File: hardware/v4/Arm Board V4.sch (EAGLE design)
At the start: 43 parts, among them U1 SN74LS241DW, U2 XBEE-1B3, U3 LSM9DS0

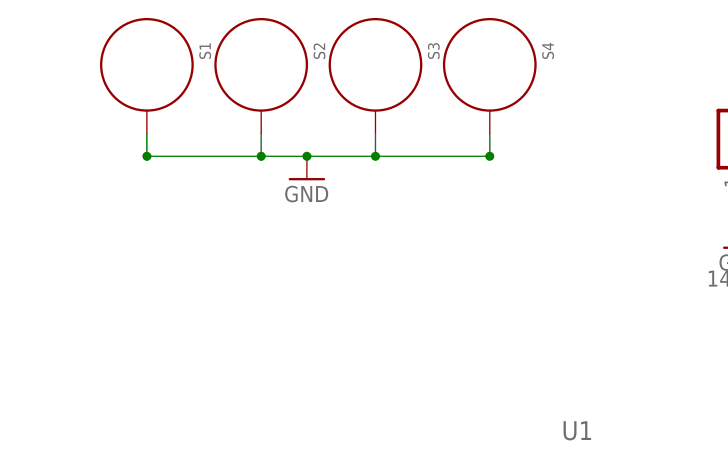
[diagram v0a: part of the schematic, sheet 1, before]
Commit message: A few small spacing changes
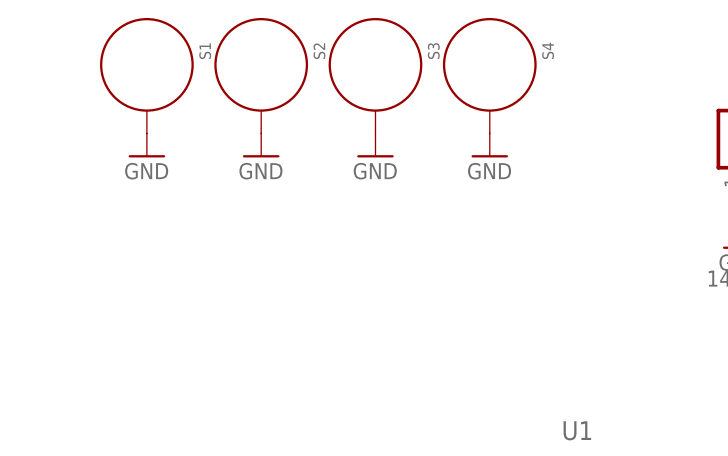
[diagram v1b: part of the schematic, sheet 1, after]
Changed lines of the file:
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@@
 <part name="GND6" library="SparkFun-Aesthetics" deviceset="GND" device=""/>
 <part name="GND9" library="SparkFun-Aesthetics" deviceset="GND" device=""/>
+<part name="GND12" library="SparkFun-Aesthetics" deviceset="GND" device=""/>
+<part name="GND13" library="SparkFun-Aesthetics" deviceset="GND" device=""/>
+<part name="GND14" library="SparkFun-Aesthetics" deviceset="GND" device=""/>
 </parts>
 <sheets>
@@
 <instance part="S3" gate="G$1" x="50.8" y="58.42" rot="R270"/>
 <instance part="S4" gate="G$1" x="63.5" y="58.42" rot="R270"/>
-<instance part="GND11" gate="1" x="43.18" y="45.72"/>
+<instance part="GND11" gate="1" x="38.1" y="48.26"/>
 <instance part="U$5" gate="G$1" x="175.26" y="10.16"/>
 <instance part="GND3" gate="1" x="175.26" y="-5.08"/>
@@
 <instance part="GND6" gate="1" x="144.78" y="15.24" rot="R90"/>
 <instance part="GND9" gate="1" x="144.78" y="-10.16" rot="R90"/>
+<instance part="GND12" gate="1" x="25.4" y="48.26"/>
+<instance part="GND13" gate="1" x="50.8" y="48.26"/>
+<instance part="GND14" gate="1" x="63.5" y="48.26"/>
 </instances>
 <busses>
@@
 </segment>
 <segment>
-<pinref part="S1" gate="G$1" pin="P$1"/>
-<wire x1="25.4" y1="50.8" x2="25.4" y2="48.26" width="0.1524" layer="91"/>
-<pinref part="GND11" gate="1" pin="GND"/>
-<wire x1="25.4" y1="48.26" x2="38.1" y2="48.26" width="0.1524" layer="91"/>
-<pinref part="S2" gate="G$1" pin="P$1"/>
-<wire x1="43.18" y1="48.26" x2="38.1" y2="48.26" width="0.1524" layer="91"/>
-<wire x1="38.1" y1="50.8" x2="38.1" y2="48.26" width="0.1524" layer="91"/>
-<pinref part="S4" gate="G$1" pin="P$1"/>
-<wire x1="63.5" y1="50.8" x2="63.5" y2="48.26" width="0.1524" layer="91"/>
-<wire x1="63.5" y1="48.26" x2="50.8" y2="48.26" width="0.1524" layer="91"/>
-<pinref part="S3" gate="G$1" pin="P$1"/>
-<wire x1="50.8" y1="48.26" x2="43.18" y2="48.26" width="0.1524" layer="91"/>
-<wire x1="50.8" y1="50.8" x2="50.8" y2="48.26" width="0.1524" layer="91"/>
-<junction x="38.1" y="48.26"/>
-<junction x="50.8" y="48.26"/>
-<junction x="43.18" y="48.26"/>
-<junction x="25.4" y="48.26"/>
-<junction x="63.5" y="48.26"/>
-</segment>
-<segment>
 <pinref part="U$5" gate="G$1" pin="C"/>
 <pinref part="GND3" gate="1" pin="GND"/>
@@
 <pinref part="GND9" gate="1" pin="GND"/>
 </segment>
+<segment>
+<pinref part="S2" gate="G$1" pin="P$1"/>
+<pinref part="GND11" gate="1" pin="GND"/>
+</segment>
+<segment>
+<pinref part="S1" gate="G$1" pin="P$1"/>
+<pinref part="GND12" gate="1" pin="GND"/>
+</segment>
+<segment>
+<pinref part="S3" gate="G$1" pin="P$1"/>
+<pinref part="GND13" gate="1" pin="GND"/>
+</segment>
+<segment>
+<pinref part="S4" gate="G$1" pin="P$1"/>
+<pinref part="GND14" gate="1" pin="GND"/>
+</segment>
 </net>

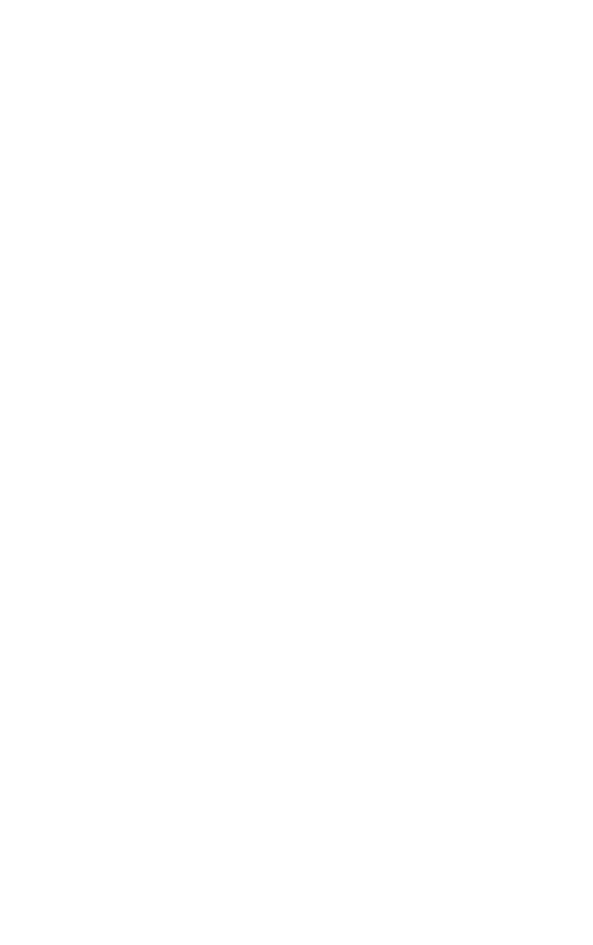
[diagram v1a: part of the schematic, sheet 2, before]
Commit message: Moving things to make room for motor controller
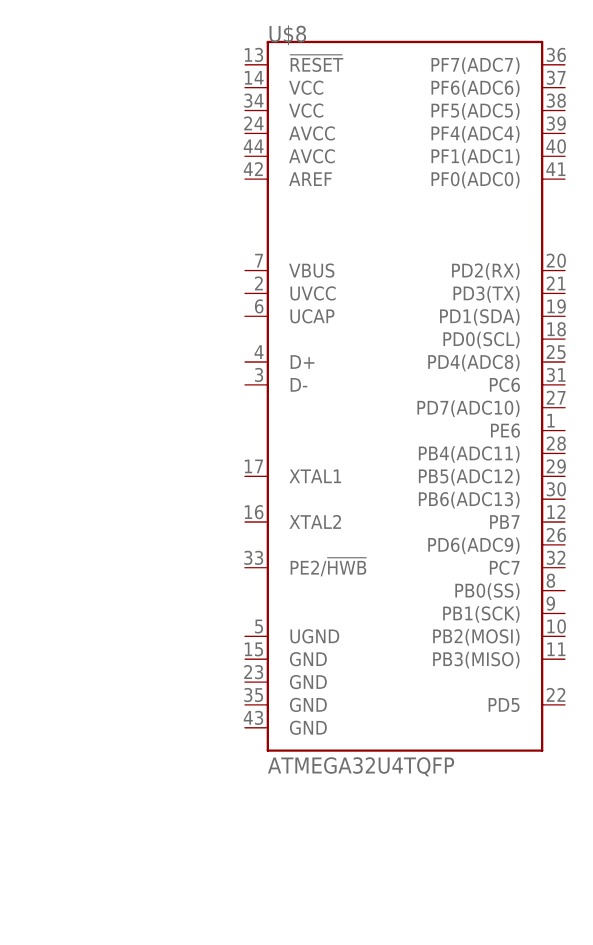
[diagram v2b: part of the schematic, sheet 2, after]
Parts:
- added U$8: ATMEGA32U4TQFP, SparkFun-DigitalIC:ATMEGA32U4TQFP
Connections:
- net +12V: no longer JP12.2
- net 14.8V: now also JP12.2
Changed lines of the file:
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@@
 <part name="GND13" library="SparkFun-Aesthetics" deviceset="GND" device=""/>
 <part name="GND14" library="SparkFun-Aesthetics" deviceset="GND" device=""/>
+<part name="U$8" library="SparkFun-DigitalIC" deviceset="ATMEGA32U4" device="TQFP"/>
 </parts>
 <sheets>
@@
 <net name="+12V" class="0">
 <segment>
-<wire x1="147.32" y1="43.18" x2="147.32" y2="35.56" width="0.1524" layer="91"/>
-<label x="147.32" y="35.56" size="1.778" layer="95" rot="R180"/>
-<pinref part="JP12" gate="G$1" pin="2"/>
-</segment>
-<segment>
 <pinref part="U$5" gate="G$1" pin="L"/>
 <wire x1="165.1" y1="12.7" x2="162.56" y2="12.7" width="0.1524" layer="91"/>
@@
 <wire x1="271.78" y1="33.02" x2="276.86" y2="33.02" width="0.1524" layer="91"/>
 <junction x="271.78" y="33.02"/>
+</segment>
+<segment>
+<wire x1="147.32" y1="43.18" x2="147.32" y2="35.56" width="0.1524" layer="91"/>
+<label x="147.32" y="35.56" size="1.778" layer="95" rot="R180"/>
+<pinref part="JP12" gate="G$1" pin="2"/>
 </segment>
 </net>
@@
 <instance part="GND8" gate="1" x="43.18" y="5.08"/>
 <instance part="U$4" gate="G$1" x="91.44" y="15.24"/>
+<instance part="U$8" gate="G$1" x="195.58" y="88.9"/>
 </instances>
 <busses>

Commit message: Stuff
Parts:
- removed U$8: ATMEGA32U4TQFP, SparkFun-DigitalIC:ATMEGA32U4TQFP
- added C2: 5.6nF, SparkFun-Capacitors:0.1UF-25V(+80/-20%)(0603)
- added C4: 220nF, SparkFun-Capacitors:0.1UF-25V-5%(0603)
- added C9: 10nF, SparkFun-Capacitors:0.1UF-25V-5%(0603)
- added D1, D2: 1N4148, SparkFun-DiscreteSemi:DIODE1N4148
- added IC3: L6206D, L6206D:L6206D
- added R15: 100, SparkFun-Passives:RESISTOR0805-RES
- added R8: 100k, SparkFun-Passives:RESISTOR0805-RES
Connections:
- new net A1: IC3.OUT1_A, U$6.L
- new net A2: IC3.OUT2_A, U$6.R
- new net EN_A: R8.2
- new net IN1_A: IC3.IN1_A
- new net IN2_A: IC3.IN2_A
- new net N$17: D1.A, D2.C, R15.2
- new net N$18: C9.2, R15.1
- new net N$19: C9.1, IC3.VCP
- new net OCD_A: C2.2, IC3.EN_A, IC3.OCD_A, R8.1
- new net VBOOT: C4.2, D1.C, IC3.VBOOT
- net +12V: now also C4.1, D2.A, IC3.VS_A, IC3.VS_B; no longer U$6.L
- net GND: now also C2.1, IC3.PROGCL_A, IC3.PROGCL_B, IC3.SENSE_A, IC3.SENSE_B; no longer U$6.R
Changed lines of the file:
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@@
 <part name="U$6" library="MRDT-2015-PowerBoard" deviceset="H_WR-TBL_32*1*0002" device="VERT"/>
 <part name="U$7" library="MRDT-2015-PowerBoard" deviceset="H_WR-TBL_32*1*0002" device="VERT"/>
-<part name="GND6" library="SparkFun-Aesthetics" deviceset="GND" device=""/>
 <part name="GND9" library="SparkFun-Aesthetics" deviceset="GND" device=""/>
 <part name="GND12" library="SparkFun-Aesthetics" deviceset="GND" device=""/>
 <part name="GND13" library="SparkFun-Aesthetics" deviceset="GND" device=""/>
 <part name="GND14" library="SparkFun-Aesthetics" deviceset="GND" device=""/>
-<part name="U$8" library="SparkFun-DigitalIC" deviceset="ATMEGA32U4" device="TQFP"/>
+<part name="IC3" library="L6206D" deviceset="L6206" device="D"/>
+<part name="GND17" library="SparkFun-Aesthetics" deviceset="GND" device=""/>
+<part name="GND39" library="SparkFun-Aesthetics" deviceset="GND" device=""/>
+<part name="GND44" library="SparkFun-Aesthetics" deviceset="GND" device=""/>
+<part name="GND46" library="SparkFun-Aesthetics" deviceset="GND" device=""/>
+<part name="R8" library="SparkFun-Passives" deviceset="RESISTOR" device="0805-RES" value="100k"/>
+<part name="C2" library="SparkFun-Capacitors" deviceset="0.1UF-25V(+80/-20%)(0603)" device="" value="5.6nF"/>
+<part name="GND47" library="SparkFun-Aesthetics" deviceset="GND" device=""/>
+<part name="D2" library="SparkFun-DiscreteSemi" deviceset="DIODE" device="1N4148" value="1N4148"/>
+<part name="D1" library="SparkFun-DiscreteSemi" deviceset="DIODE" device="1N4148" value="1N4148"/>
+<part name="C4" library="SparkFun-Capacitors" deviceset="0.1UF-25V-5%(0603)" device="" value="220nF"/>
+<part name="C9" library="SparkFun-Capacitors" deviceset="0.1UF-25V-5%(0603)" device="" value="10nF"/>
+<part name="R15" library="SparkFun-Passives" deviceset="RESISTOR" device="0805-RES" value="100"/>
 </parts>
 <sheets>
@@
 <instance part="U$6" gate="G$1" x="132.08" y="12.7"/>
 <instance part="U$7" gate="G$1" x="132.08" y="-12.7"/>
-<instance part="GND6" gate="1" x="144.78" y="15.24" rot="R90"/>
 <instance part="GND9" gate="1" x="144.78" y="-10.16" rot="R90"/>
 <instance part="GND12" gate="1" x="25.4" y="48.26"/>
@@
 </segment>
 <segment>
-<pinref part="U$6" gate="G$1" pin="R"/>
-<pinref part="GND6" gate="1" pin="GND"/>
-</segment>
-<segment>
 <pinref part="U$7" gate="G$1" pin="R"/>
 <pinref part="GND9" gate="1" pin="GND"/>
@@
 <wire x1="162.56" y1="12.7" x2="162.56" y2="15.24" width="0.1524" layer="91"/>
 <label x="162.56" y="15.24" size="1.778" layer="95"/>
-</segment>
-<segment>
-<pinref part="U$6" gate="G$1" pin="L"/>
-<wire x1="121.92" y1="15.24" x2="116.84" y2="15.24" width="0.1524" layer="91"/>
-<label x="116.84" y="15.24" size="1.778" layer="95"/>
 </segment>
 <segment>
@@
 <pinref part="R9" gate="G$1" pin="1"/>
 <pinref part="LED5" gate="G$1" pin="A"/>
+</segment>
+</net>
+<net name="A1" class="0">
+<segment>
+<pinref part="U$6" gate="G$1" pin="L"/>
+<wire x1="121.92" y1="15.24" x2="116.84" y2="15.24" width="0.1524" layer="91"/>
+<label x="116.84" y="15.24" size="1.778" layer="95"/>
+</segment>
+</net>
+<net name="A2" class="0">
+<segment>
+<pinref part="U$6" gate="G$1" pin="R"/>
+<wire x1="142.24" y1="15.24" x2="147.32" y2="15.24" width="0.1524" layer="91"/>
+<label x="147.32" y="15.24" size="1.778" layer="95"/>
 </segment>
 </net>
@@
 <instance part="GND8" gate="1" x="43.18" y="5.08"/>
 <instance part="U$4" gate="G$1" x="91.44" y="15.24"/>
-<instance part="U$8" gate="G$1" x="195.58" y="88.9"/>
 </instances>
 <busses>
@@
 </segment>
 </net>
+</nets>
+</sheet>
+<sheet>
+<plain>
+</plain>
+<instances>
+<instance part="IC3" gate="G$1" x="27.94" y="17.78"/>
+<instance part="GND17" gate="1" x="2.54" y="27.94" rot="R270"/>
+<instance part="GND39" gate="1" x="2.54" y="10.16" rot="R270"/>
+<instance part="GND44" gate="1" x="45.72" y="33.02" rot="R90"/>
+<instance part="GND46" gate="1" x="45.72" y="5.08" rot="R90"/>
+<instance part="R8" gate="G$1" x="81.28" y="30.48"/>
+<instance part="C2" gate="G$1" x="73.66" y="35.56"/>
+<instance part="GND47" gate="1" x="86.36" y="40.64" rot="R90"/>
+<instance part="D2" gate="G$1" x="68.58" y="17.78" rot="R90"/>
+<instance part="D1" gate="G$1" x="73.66" y="22.86"/>
+<instance part="C4" gate="G$1" x="78.74" y="20.32" rot="R180"/>
+<instance part="C9" gate="G$1" x="53.34" y="27.94" rot="R90"/>
+<instance part="R15" gate="G$1" x="60.96" y="22.86"/>
+</instances>
+<busses>
+</busses>
+<nets>
+<net name="A1" class="0">
+<segment>
+<pinref part="IC3" gate="G$1" pin="OUT1_A"/>
+<wire x1="12.7" y1="22.86" x2="10.16" y2="22.86" width="0.1524" layer="91"/>
+<label x="7.62" y="22.86" size="1.778" layer="95"/>
+</segment>
+</net>
+<net name="A2" class="0">
+<segment>
+<pinref part="IC3" gate="G$1" pin="OUT2_A"/>
+<wire x1="43.18" y1="25.4" x2="45.72" y2="25.4" width="0.1524" layer="91"/>
+<label x="45.72" y="25.4" size="1.778" layer="95"/>
+</segment>
+</net>
+<net name="GND" class="0">
+<segment>
+<pinref part="IC3" gate="G$1" pin="SENSE_A"/>
+<pinref part="GND17" gate="1" pin="GND"/>
+<wire x1="5.08" y1="27.94" x2="12.7" y2="27.94" width="0.1524" layer="91"/>
+</segment>
+<segment>
+<pinref part="IC3" gate="G$1" pin="SENSE_B"/>
+<pinref part="GND39" gate="1" pin="GND"/>
+<wire x1="5.08" y1="10.16" x2="12.7" y2="10.16" width="0.1524" layer="91"/>
+</segment>
+<segment>
+<pinref part="IC3" gate="G$1" pin="PROGCL_A"/>
+<pinref part="GND44" gate="1" pin="GND"/>
+</segment>
+<segment>
+<pinref part="IC3" gate="G$1" pin="PROGCL_B"/>
+<pinref part="GND46" gate="1" pin="GND"/>
+</segment>
+<segment>
+<pinref part="C2" gate="G$1" pin="1"/>
+<pinref part="GND47" gate="1" pin="GND"/>
+<wire x1="83.82" y1="40.64" x2="73.66" y2="40.64" width="0.1524" layer="91"/>
+</segment>
+</net>
+<net name="IN1_A" class="0">
+<segment>
+<pinref part="IC3" gate="G$1" pin="IN1_A"/>
+<wire x1="12.7" y1="33.02" x2="10.16" y2="33.02" width="0.1524" layer="91"/>
+<label x="2.54" y="33.02" size="1.778" layer="95"/>
+</segment>
+</net>
+<net name="IN2_A" class="0">
+<segment>
+<pinref part="IC3" gate="G$1" pin="IN2_A"/>
+<wire x1="12.7" y1="30.48" x2="10.16" y2="30.48" width="0.1524" layer="91"/>
+<label x="2.54" y="30.48" size="1.778" layer="95"/>
+</segment>
+</net>
+<net name="N$17" class="0">
+<segment>
+<pinref part="D2" gate="G$1" pin="C"/>
+<wire x1="68.58" y1="20.32" x2="68.58" y2="22.86" width="0.1524" layer="91"/>
+<pinref part="D1" gate="G$1" pin="A"/>
+<wire x1="68.58" y1="22.86" x2="71.12" y2="22.86" width="0.1524" layer="91"/>
+<pinref part="R15" gate="G$1" pin="2"/>
+<wire x1="66.04" y1="22.86" x2="68.58" y2="22.86" width="0.1524" layer="91"/>
+<junction x="68.58" y="22.86"/>
+</segment>
+</net>
+<net name="N$18" class="0">
+<segment>
+<pinref part="C9" gate="G$1" pin="2"/>
+<pinref part="R15" gate="G$1" pin="1"/>
+<wire x1="55.88" y1="22.86" x2="55.88" y2="27.94" width="0.1524" layer="91"/>
+</segment>
+</net>
+<net name="N$19" class="0">
+<segment>
+<pinref part="C9" gate="G$1" pin="1"/>
+<pinref part="IC3" gate="G$1" pin="VCP"/>
+<wire x1="48.26" y1="27.94" x2="43.18" y2="27.94" width="0.1524" layer="91"/>
+</segment>
+</net>
+<net name="EN_A" class="0">
+<segment>
+<pinref part="R8" gate="G$1" pin="2"/>
+<wire x1="86.36" y1="30.48" x2="88.9" y2="30.48" width="0.1524" layer="91"/>
+<label x="88.9" y="30.48" size="1.778" layer="95"/>
+</segment>
+</net>
+<net name="+12V" class="0">
+<segment>
+<pinref part="C4" gate="G$1" pin="1"/>
+<wire x1="78.74" y1="15.24" x2="68.58" y2="15.24" width="0.1524" layer="91"/>
+<pinref part="D2" gate="G$1" pin="A"/>
+<wire x1="78.74" y1="15.24" x2="88.9" y2="15.24" width="0.1524" layer="91"/>
+<junction x="78.74" y="15.24"/>
+<label x="88.9" y="15.24" size="1.778" layer="95"/>
+<wire x1="68.58" y1="15.24" x2="45.72" y2="15.24" width="0.1524" layer="91"/>
+<pinref part="IC3" gate="G$1" pin="VS_B"/>
+<pinref part="IC3" gate="G$1" pin="VS_A"/>
+<wire x1="45.72" y1="15.24" x2="43.18" y2="15.24" width="0.1524" layer="91"/>
+<wire x1="43.18" y1="22.86" x2="45.72" y2="22.86" width="0.1524" layer="91"/>
+<wire x1="45.72" y1="22.86" x2="45.72" y2="15.24" width="0.1524" layer="91"/>
+<junction x="45.72" y="15.24"/>
+<junction x="68.58" y="15.24"/>
+</segment>
+</net>
+<net name="OCD_A" class="0">
+<segment>
+<pinref part="IC3" gate="G$1" pin="OCD_A"/>
+<wire x1="12.7" y1="25.4" x2="10.16" y2="25.4" width="0.1524" layer="91"/>
+<label x="2.54" y="25.4" size="1.778" layer="95"/>
+</segment>
+<segment>
+<pinref part="R8" gate="G$1" pin="1"/>
+<wire x1="76.2" y1="30.48" x2="73.66" y2="30.48" width="0.1524" layer="91"/>
+<pinref part="C2" gate="G$1" pin="2"/>
+<wire x1="73.66" y1="30.48" x2="73.66" y2="33.02" width="0.1524" layer="91"/>
+<junction x="73.66" y="30.48"/>
+<wire x1="73.66" y1="30.48" x2="73.66" y2="27.94" width="0.1524" layer="91"/>
+<wire x1="73.66" y1="27.94" x2="78.74" y2="27.94" width="0.1524" layer="91"/>
+<label x="78.74" y="27.94" size="1.778" layer="95"/>
+<pinref part="IC3" gate="G$1" pin="EN_A"/>
+<wire x1="73.66" y1="30.48" x2="43.18" y2="30.48" width="0.1524" layer="91"/>
+</segment>
+</net>
+<net name="VBOOT" class="0">
+<segment>
+<pinref part="D1" gate="G$1" pin="C"/>
+<pinref part="C4" gate="G$1" pin="2"/>
+<wire x1="76.2" y1="22.86" x2="78.74" y2="22.86" width="0.1524" layer="91"/>
+<junction x="78.74" y="22.86"/>
+<wire x1="78.74" y1="22.86" x2="88.9" y2="22.86" width="0.1524" layer="91"/>
+<label x="88.9" y="22.86" size="1.778" layer="95"/>
+</segment>
+<segment>
+<pinref part="IC3" gate="G$1" pin="VBOOT"/>
+<wire x1="43.18" y1="10.16" x2="45.72" y2="10.16" width="0.1524" layer="91"/>
+<label x="45.72" y="10.16" size="1.778" layer="95"/>
+</segment>
+</net>

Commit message: More stuff
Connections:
- removed net LA_PWM: JP7.3, U$1.PB6
- removed net PWM1: U$1.PD1
- removed net PWM2: U$1.PD2
- removed net PWM3: U$1.PD3
- removed net RX_7: U$1.PE0
- removed net TX_7: U$1.PE1
- new net LA_ENC: JP7.3, U$1.PE3
- net +3V3: now also JP7.2
- net +5V: no longer JP7.2
- net EN_A: now also U$1.PD3
- net IN1_A: now also U$1.PE1
- net IN2_A: now also U$1.PE2
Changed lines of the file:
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@@
 <?xml version="1.0" encoding="utf-8"?>
 <!DOCTYPE eagle SYSTEM "eagle.dtd">
-<eagle version="6.5.0">
+<eagle version="7.1.0">
 <drawing>
 <settings>
@@
 <label x="50.8" y="7.62" size="1.778" layer="95"/>
 </segment>
-<segment>
-<pinref part="JP7" gate="G$1" pin="2"/>
-<wire x1="190.5" y1="43.18" x2="190.5" y2="38.1" width="0.1524" layer="91"/>
-<label x="190.5" y="38.1" size="1.778" layer="95" rot="R180"/>
-</segment>
 </net>
 <net name="14.8V" class="0">
@@
 </segment>
 </net>
-<net name="LA_PWM" class="0">
+<net name="LA_ENC" class="0">
 <segment>
 <pinref part="JP7" gate="G$1" pin="3"/>
@@
 <wire x1="142.24" y1="15.24" x2="147.32" y2="15.24" width="0.1524" layer="91"/>
 <label x="147.32" y="15.24" size="1.778" layer="95"/>
+</segment>
+</net>
+<net name="+3V3" class="0">
+<segment>
+<pinref part="JP7" gate="G$1" pin="2"/>
+<wire x1="190.5" y1="43.18" x2="190.5" y2="38.1" width="0.1524" layer="91"/>
+<label x="190.5" y="38.1" size="1.778" layer="95" rot="R180"/>
 </segment>
 </net>
@@
 </segment>
 </net>
-<net name="RX_7" class="0">
-<segment>
-<pinref part="U$1" gate="G$1" pin="PE0"/>
-<wire x1="10.16" y1="33.02" x2="5.08" y2="33.02" width="0.1524" layer="91"/>
-<label x="2.54" y="33.02" size="1.778" layer="95"/>
-</segment>
-</net>
-<net name="TX_7" class="0">
-<segment>
-<pinref part="U$1" gate="G$1" pin="PE1"/>
-<wire x1="10.16" y1="30.48" x2="5.08" y2="30.48" width="0.1524" layer="91"/>
-<label x="2.54" y="30.48" size="1.778" layer="95"/>
-</segment>
-</net>
 <net name="RX_5" class="0">
 <segment>
@@
 </segment>
 </net>
-<net name="LA_PWM" class="0">
-<segment>
-<pinref part="U$1" gate="G$1" pin="PB6"/>
-<wire x1="40.64" y1="63.5" x2="45.72" y2="63.5" width="0.1524" layer="91"/>
-<label x="43.18" y="63.5" size="1.778" layer="95"/>
-</segment>
-</net>
-<net name="PWM3" class="0">
-<segment>
-<pinref part="U$1" gate="G$1" pin="PD3"/>
-<wire x1="40.64" y1="48.26" x2="45.72" y2="48.26" width="0.1524" layer="91"/>
-</segment>
-</net>
-<net name="PWM2" class="0">
-<segment>
-<pinref part="U$1" gate="G$1" pin="PD2"/>
-<wire x1="40.64" y1="50.8" x2="45.72" y2="50.8" width="0.1524" layer="91"/>
-</segment>
-</net>
-<net name="PWM1" class="0">
-<segment>
-<pinref part="U$1" gate="G$1" pin="PD1"/>
-<wire x1="40.64" y1="53.34" x2="45.72" y2="53.34" width="0.1524" layer="91"/>
-</segment>
-</net>
 <net name="SCL" class="0">
 <segment>
 <pinref part="U$1" gate="G$1" pin="PA6"/>
 <wire x1="10.16" y1="63.5" x2="2.54" y2="63.5" width="0.1524" layer="91"/>
+<label x="2.54" y="63.5" size="1.778" layer="95"/>
 </segment>
 </net>
@@
 <pinref part="U$1" gate="G$1" pin="PA7"/>
 <wire x1="10.16" y1="60.96" x2="2.54" y2="60.96" width="0.1524" layer="91"/>
+<label x="2.54" y="60.96" size="1.778" layer="95"/>
 </segment>
 </net>
@@
 <pinref part="U$1" gate="G$1" pin="VBUS"/>
 <wire x1="10.16" y1="7.62" x2="5.08" y2="7.62" width="0.1524" layer="91"/>
+<label x="2.54" y="7.62" size="1.778" layer="95"/>
 </segment>
 <segment>
@@
 </segment>
 </net>
+<net name="LA_ENC" class="0">
+<segment>
+<pinref part="U$1" gate="G$1" pin="PE3"/>
+<wire x1="10.16" y1="25.4" x2="5.08" y2="25.4" width="0.1524" layer="91"/>
+<label x="-2.54" y="25.4" size="1.778" layer="95"/>
+</segment>
+</net>
+<net name="IN1_A" class="0">
+<segment>
+<pinref part="U$1" gate="G$1" pin="PE1"/>
+<wire x1="10.16" y1="30.48" x2="5.08" y2="30.48" width="0.1524" layer="91"/>
+</segment>
+</net>
+<net name="EN_A" class="0">
+<segment>
+<pinref part="U$1" gate="G$1" pin="PD3"/>
+<wire x1="40.64" y1="48.26" x2="45.72" y2="48.26" width="0.1524" layer="91"/>
+</segment>
+</net>
+<net name="IN2_A" class="0">
+<segment>
+<pinref part="U$1" gate="G$1" pin="PE2"/>
+<wire x1="10.16" y1="27.94" x2="5.08" y2="27.94" width="0.1524" layer="91"/>
+</segment>
+</net>
